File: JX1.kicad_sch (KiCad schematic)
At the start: 1 part

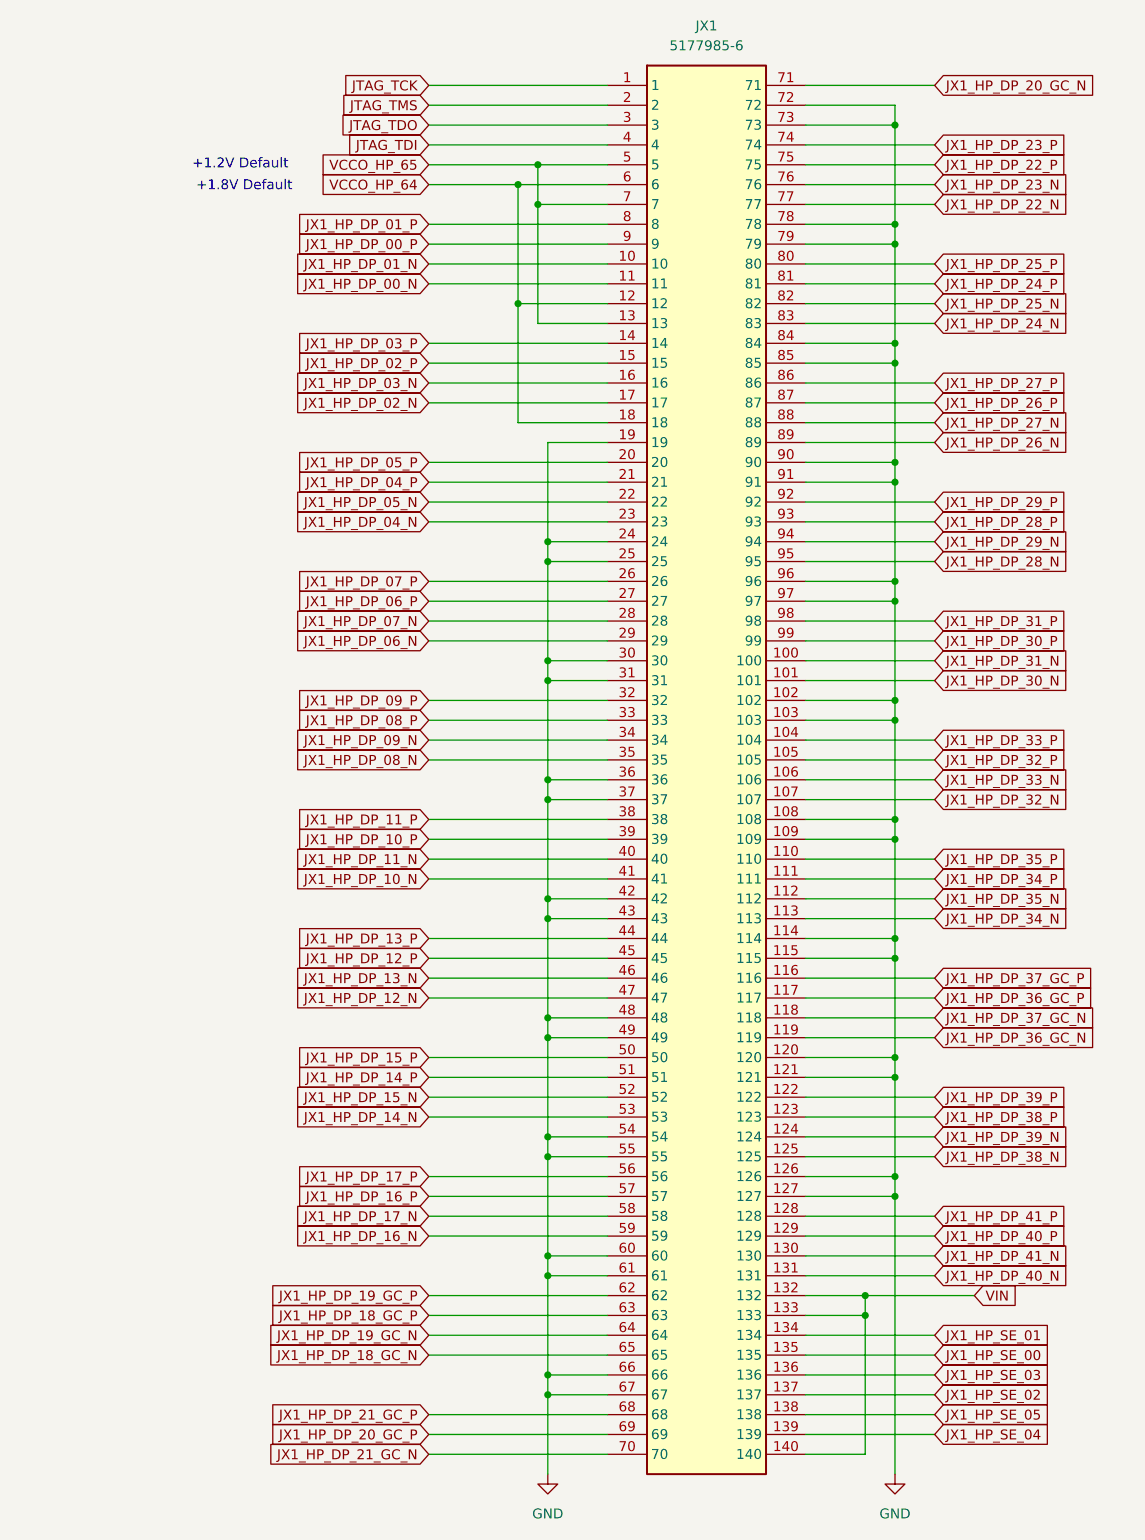
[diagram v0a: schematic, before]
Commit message: moved jtag connector, added holes for all power supplies, fixed most of DRC
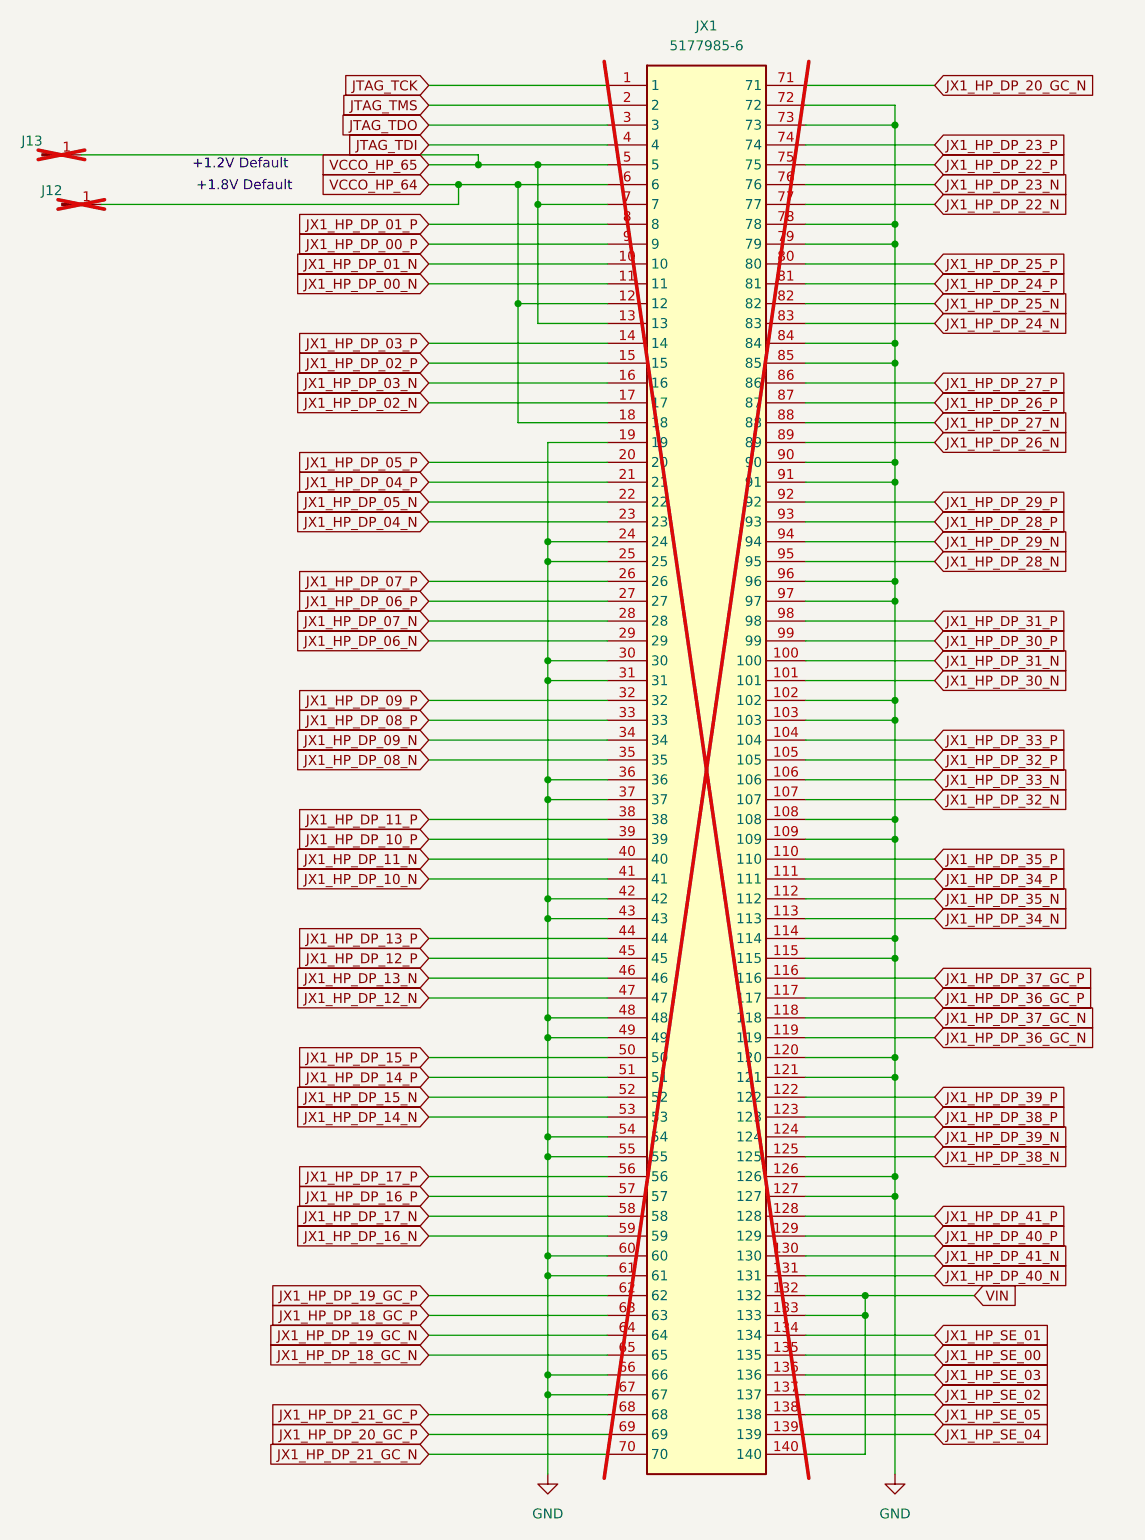
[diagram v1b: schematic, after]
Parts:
- added J12, J13: Conn_01x01_Pin, Connector_PinHeader_2.00mm:PinHeader_1x01_P2.00mm_Horizontal, symbol Connector:Conn_01x01_Pin
- JX1: now not fitted
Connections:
- net VCCO_HP_64: now also J12.1 (Pin_1)
- net VCCO_HP_65: now also J13.1 (Pin_1)
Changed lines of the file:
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@@
 	)
 	(junction
+		(at 99.06 31.75)
+		(diameter 0)
+		(color 0 0 0 0)
+	)
+	(junction
 		(at 154.94 36.83)
 		(diameter 0)
@@
 	)
 	(junction
+		(at 101.6 29.21)
+		(diameter 0)
+		(color 0 0 0 0)
+	)
+	(junction
 		(at 154.94 24.13)
 		(diameter 0)
@@
 	(wire
 		(pts
+			(xy 53.34 34.29) (xy 99.06 34.29)
+		)
+		(stroke
+			(width 0)
+			(type default)
+		)
+	)
+	(wire
+		(pts
 			(xy 109.22 49.53) (xy 109.22 34.29)
 		)
@@
 	(wire
 		(pts
+			(xy 99.06 34.29) (xy 99.06 31.75)
+		)
+		(stroke
+			(width 0)
+			(type default)
+		)
+	)
+	(wire
+		(pts
 			(xy 143.51 100.33) (xy 154.94 100.33)
 		)
@@
 	(wire
 		(pts
-			(xy 95.25 31.75) (xy 106.68 31.75)
+			(xy 95.25 31.75) (xy 99.06 31.75)
 		)
 		(stroke
@@
 	(wire
 		(pts
+			(xy 99.06 31.75) (xy 106.68 31.75)
+		)
+		(stroke
+			(width 0)
+			(type default)
+		)
+	)
+	(wire
+		(pts
 			(xy 143.51 128.27) (xy 154.94 128.27)
 		)
@@
 	(wire
 		(pts
+			(xy 50.8 27.94) (xy 101.6 27.94)
+		)
+		(stroke
+			(width 0)
+			(type default)
+		)
+	)
+	(wire
+		(pts
 			(xy 110.49 153.67) (xy 110.49 156.21)
 		)
@@
 	(wire
 		(pts
+			(xy 101.6 27.94) (xy 101.6 29.21)
+		)
+		(stroke
+			(width 0)
+			(type default)
+		)
+	)
+	(wire
+		(pts
 			(xy 110.49 168.91) (xy 118.11 168.91)
 		)
@@
 	(wire
 		(pts
+			(xy 101.6 29.21) (xy 109.22 29.21)
+		)
+		(stroke
+			(width 0)
+			(type default)
+		)
+	)
+	(wire
+		(pts
 			(xy 143.51 102.87) (xy 160.02 102.87)
 		)
@@
 	(wire
 		(pts
-			(xy 95.25 29.21) (xy 109.22 29.21)
+			(xy 95.25 29.21) (xy 101.6 29.21)
 		)
 		(stroke
@@
 	)
 	(symbol
+		(lib_id "Connector:Conn_01x01_Pin")
+		(at 45.72 27.94 0)
+		(unit 1)
+		(exclude_from_sim no)
+		(in_bom yes)
+		(on_board yes)
+		(dnp yes)
+		(property "Reference" "J13"
+			(at 44.45 26.162 0)
+			(effects
+				(font
+					(size 1.27 1.27)
+				)
+			)
+		)
+		(property "Value" "Conn_01x01_Pin"
+			(at 32.766 29.464 0)
+			(effects
+				(font
+					(size 1.27 1.27)
+				)
+				(hide yes)
+			)
+		)
+		(property "Footprint" "Connector_PinHeader_2.00mm:PinHeader_1x01_P2.00mm_Horizontal"
+			(at 45.72 27.94 0)
+			(effects
+				(font
+					(size 1.27 1.27)
+				)
+				(hide yes)
+			)
+		)
+		(property "Datasheet" "~"
+			(at 45.72 27.94 0)
+			(effects
+				(font
+					(size 1.27 1.27)
+				)
+				(hide yes)
+			)
+		)
+		(property "Description" "Generic connector, single row, 01x01, script generated"
+			(at 45.72 27.94 0)
+			(effects
+				(font
+					(size 1.27 1.27)
+				)
+				(hide yes)
+			)
+		)
+		(pin "1"
+		)
+		(instances
+			(project "simpleCarrier"
+				(path "/72db9dae-5f31-4a10-9047-fdf9bc345a06/e6ab9ad1-f986-4be7-aa63-cdcaaf3d5729"
+					(reference "J13")
+					(unit 1)
+				)
+			)
+		)
+	)
+	(symbol
+		(lib_id "Connector:Conn_01x01_Pin")
+		(at 48.26 34.29 0)
+		(unit 1)
+		(exclude_from_sim no)
+		(in_bom yes)
+		(on_board yes)
+		(dnp yes)
+		(property "Reference" "J12"
+			(at 46.99 32.512 0)
+			(effects
+				(font
+					(size 1.27 1.27)
+				)
+			)
+		)
+		(property "Value" "Conn_01x01_Pin"
+			(at 35.306 35.814 0)
+			(effects
+				(font
+					(size 1.27 1.27)
+				)
+				(hide yes)
+			)
+		)
+		(property "Footprint" "Connector_PinHeader_2.00mm:PinHeader_1x01_P2.00mm_Horizontal"
+			(at 48.26 34.29 0)
+			(effects
+				(font
+					(size 1.27 1.27)
+				)
+				(hide yes)
+			)
+		)
+		(property "Datasheet" "~"
+			(at 48.26 34.29 0)
+			(effects
+				(font
+					(size 1.27 1.27)
+				)
+				(hide yes)
+			)
+		)
+		(property "Description" "Generic connector, single row, 01x01, script generated"
+			(at 48.26 34.29 0)
+			(effects
+				(font
+					(size 1.27 1.27)
+				)
+				(hide yes)
+			)
+		)
+		(pin "1"
+		)
+		(instances
+			(project ""
+				(path "/72db9dae-5f31-4a10-9047-fdf9bc345a06/e6ab9ad1-f986-4be7-aa63-cdcaaf3d5729"
+					(reference "J12")
+					(unit 1)
+				)
+			)
+		)
+	)
+	(symbol
 		(lib_id "power:GND")
 		(at 110.49 196.85 0)
@@
 		(in_bom yes)
 		(on_board yes)
-		(dnp no)
+		(dnp yes)
 		(fields_autoplaced yes)
 		(property "Reference" "JX1"
